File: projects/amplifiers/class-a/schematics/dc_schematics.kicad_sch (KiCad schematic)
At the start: 7 parts, among them J1 5V, Q2 BC547

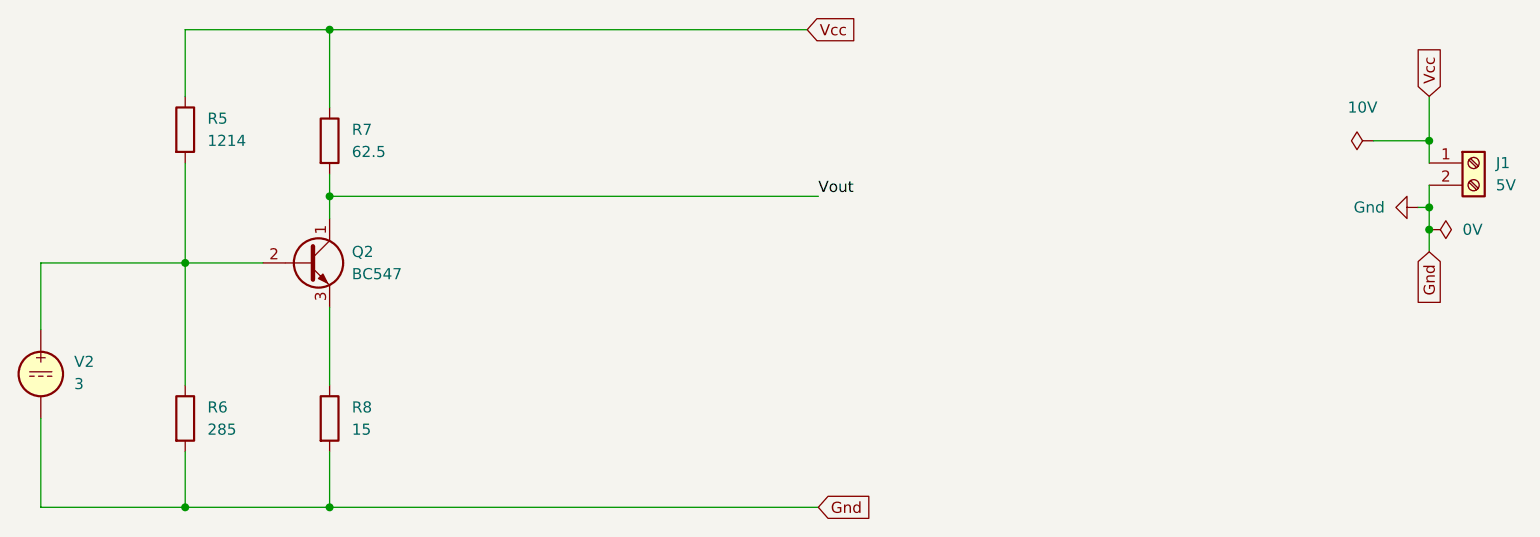
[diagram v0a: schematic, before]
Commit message: feat: Add AC analysis and simulations to Class-A amplifier
Adds AC circuit schematic with coupling/bypass capacitors
Includes AC simulation showing proper sine wave output
Document clipping behavior with excessive input amplitude
Update goals to separate DC and AC analysis tasks

Breaking changes: None

Resolves: None
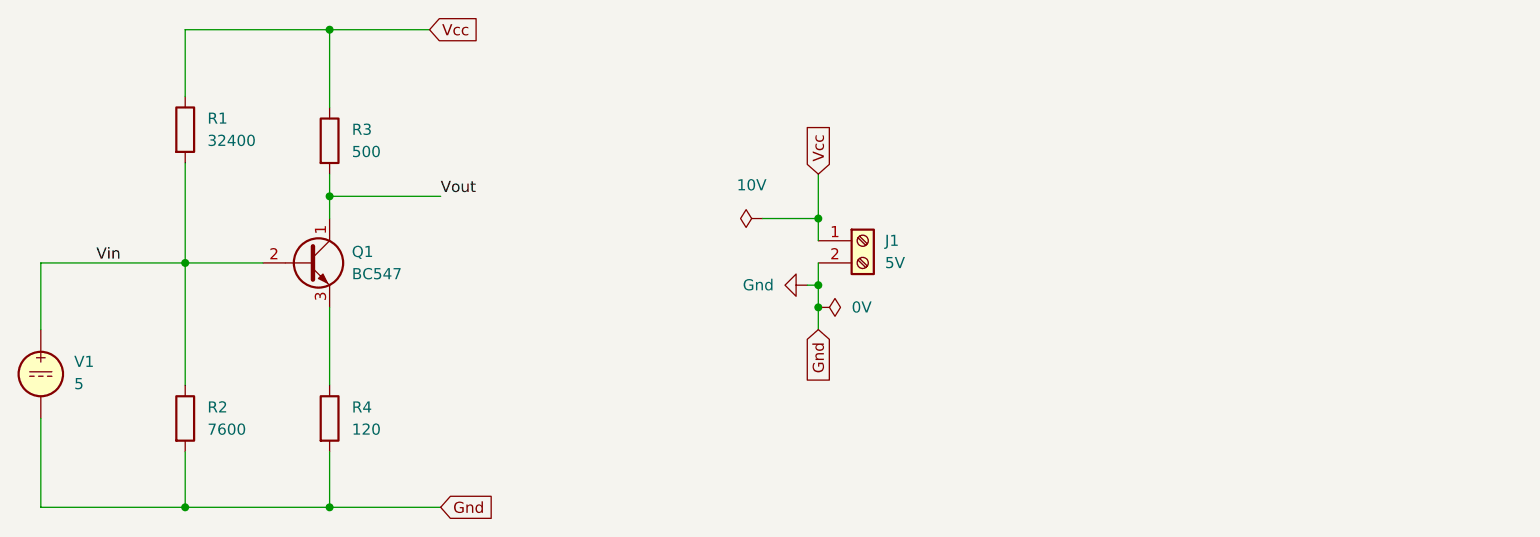
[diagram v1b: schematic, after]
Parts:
- R1: renamed from R5; value 1214 -> 32400
- R2: renamed from R6; value 285 -> 7600
- R3: renamed from R7; value 62.5 -> 500
- R4: renamed from R8; value 15 -> 120
- V1: renamed from V2; value 3 -> 5
- renumbered Q2 to Q1
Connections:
- net Vin: now reaches Q1.2 (B), R1.2, R2.1, V1.1
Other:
- moved on the sheet: J1
